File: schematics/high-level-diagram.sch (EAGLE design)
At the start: 2 parts

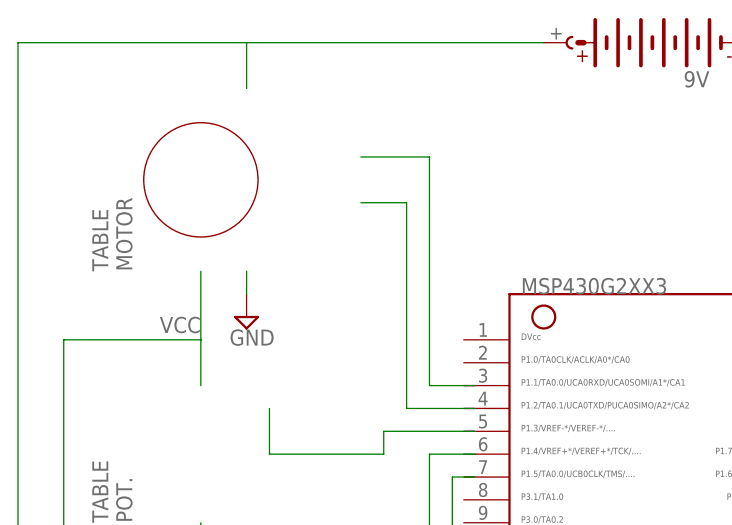
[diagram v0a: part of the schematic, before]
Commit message: Added button schematic and updated final report draft accordingly.  Adjusted high-level schematic accordingly.
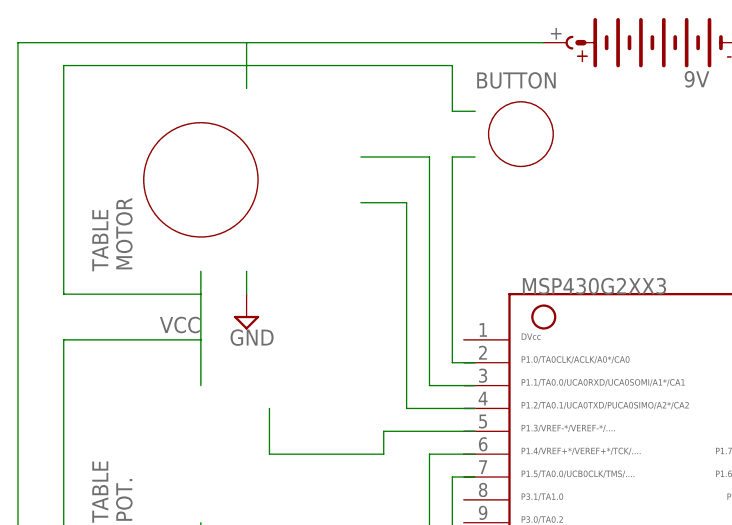
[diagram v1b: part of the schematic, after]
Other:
- note added: "BUTTON"
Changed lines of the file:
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@@
 <text x="-203.2" y="149.86" size="1.778" layer="95" rot="R90">WEAPON
 POT.</text>
+<frame x1="-165.1" y1="215.9" x2="-154.94" y2="226.06" columns="0" rows="0" layer="94" border-left="no" border-top="no" border-right="no" border-bottom="no"/>
+<circle x="-160.02" y="220.98" radius="3.5921" width="0.1524" layer="94"/>
+<text x="-165.1" y="226.06" size="1.778" layer="95">BUTTON</text>
 </plain>
 <instances>
@@
 <net name="VCC" class="0">
 <segment>
-<wire x1="-195.58" y1="205.74" x2="-195.58" y2="198.12" width="0.1524" layer="91"/>
+<wire x1="-195.58" y1="205.74" x2="-195.58" y2="203.2" width="0.1524" layer="91"/>
 <label x="-195.58" y="200.66" size="1.778" layer="95" rot="R180"/>
+<wire x1="-195.58" y1="203.2" x2="-195.58" y2="198.12" width="0.1524" layer="91"/>
 <wire x1="-195.58" y1="198.12" x2="-195.58" y2="193.04" width="0.1524" layer="91"/>
 <wire x1="-195.58" y1="198.12" x2="-210.82" y2="198.12" width="0.1524" layer="91"/>
@@
 <wire x1="-210.82" y1="167.64" x2="-195.58" y2="167.64" width="0.1524" layer="91"/>
 <wire x1="-195.58" y1="167.64" x2="-195.58" y2="165.1" width="0.1524" layer="91"/>
+<wire x1="-195.58" y1="203.2" x2="-210.82" y2="203.2" width="0.1524" layer="91"/>
+<wire x1="-210.82" y1="203.2" x2="-210.82" y2="228.6" width="0.1524" layer="91"/>
+<wire x1="-210.82" y1="228.6" x2="-167.64" y2="228.6" width="0.1524" layer="91"/>
+<wire x1="-167.64" y1="228.6" x2="-167.64" y2="223.52" width="0.1524" layer="91"/>
+<wire x1="-167.64" y1="223.52" x2="-165.1" y2="223.52" width="0.1524" layer="91"/>
 </segment>
 </net>
@@
 </segment>
 </net>
+<net name="N$4" class="0">
+<segment>
+<wire x1="-165.1" y1="218.44" x2="-167.64" y2="218.44" width="0.1524" layer="91"/>
+<wire x1="-167.64" y1="218.44" x2="-167.64" y2="195.58" width="0.1524" layer="91"/>
+<wire x1="-167.64" y1="195.58" x2="-165.1" y2="195.58" width="0.1524" layer="91"/>
+</segment>
+</net>

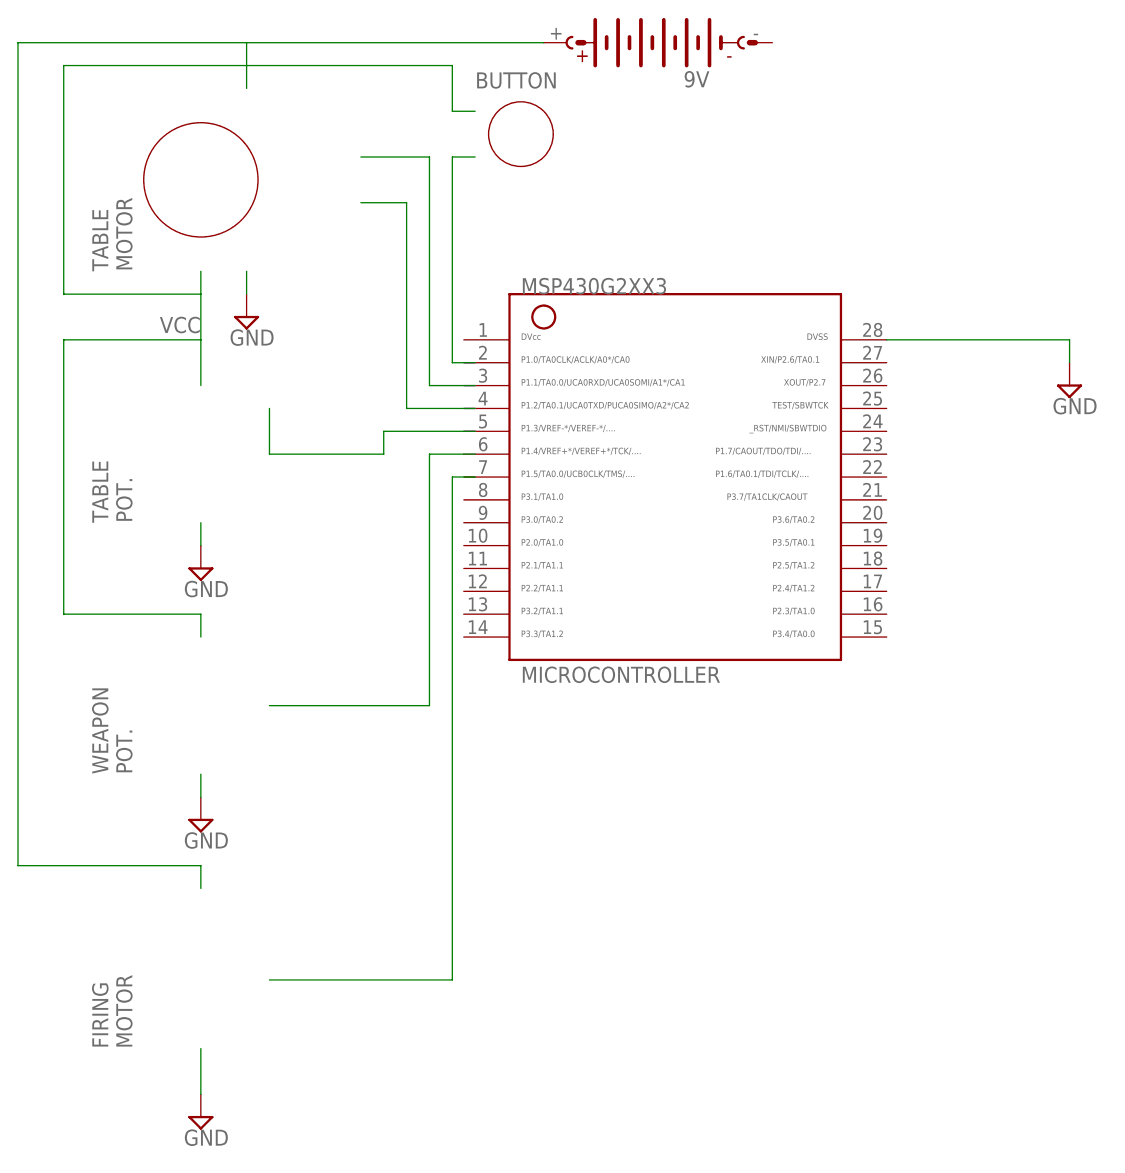
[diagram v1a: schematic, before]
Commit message: Updated schematics to have appropriate pins and to fit most recent updates.  Final report updated and ready for review.
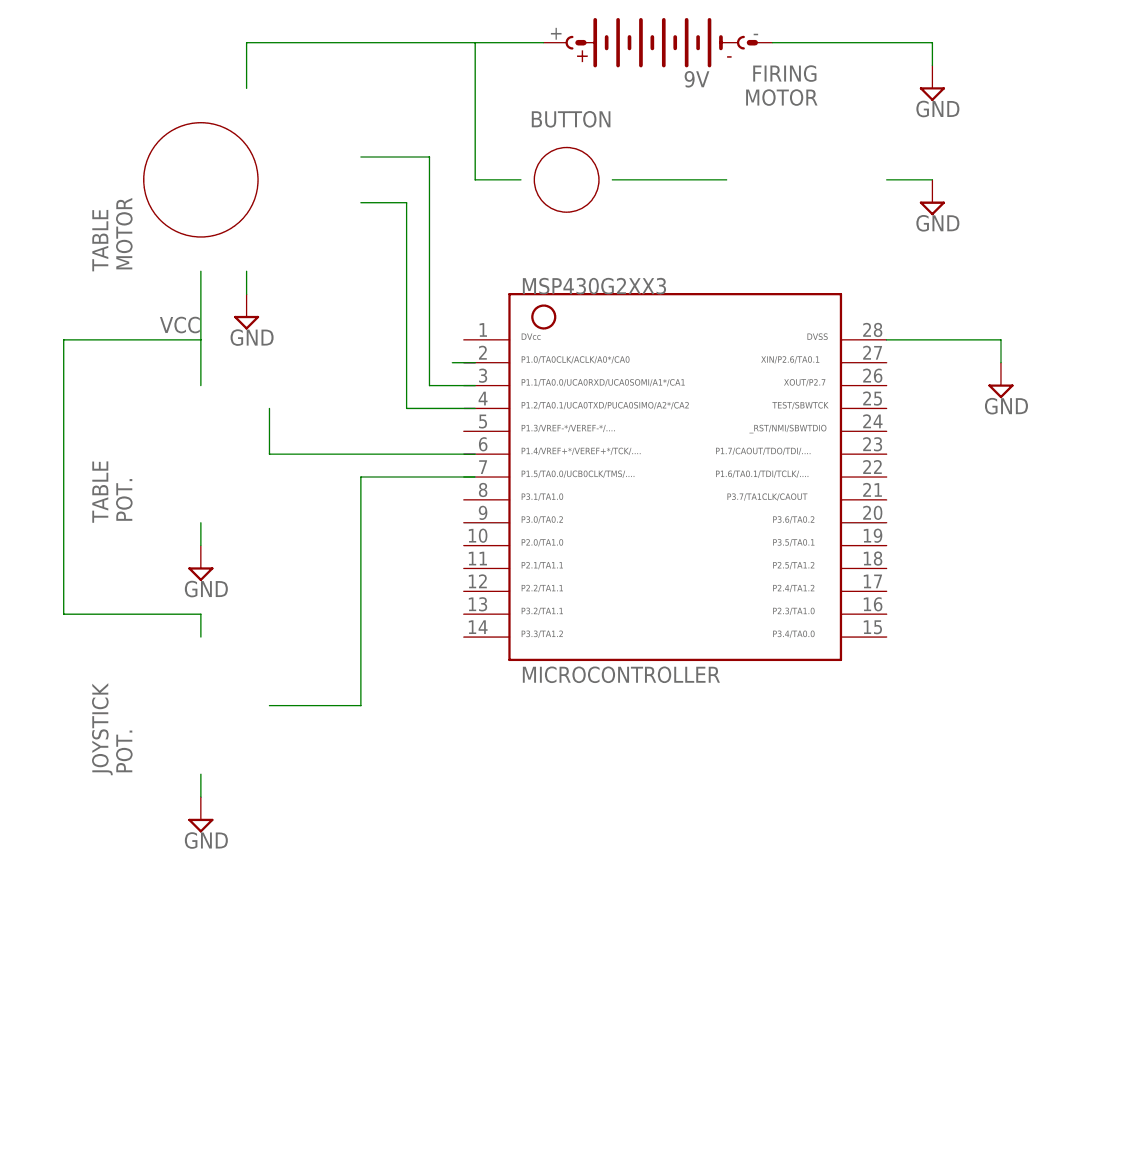
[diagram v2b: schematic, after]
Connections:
- net GND: now also 9V.-
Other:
- note added: "JOYSTICK POT."
- note removed: "WEAPON POT."
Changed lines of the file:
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@@
 <part name="SUPPLY1" library="supply2" deviceset="GND" device=""/>
 <part name="SUPPLY2" library="supply2" deviceset="GND" device=""/>
+<part name="SUPPLY3" library="supply2" deviceset="GND" device=""/>
 </parts>
 <sheets>
@@
 MOTOR</text>
 <circle x="-195.58" y="215.9" radius="6.35" width="0.1524" layer="94"/>
-<frame x1="-203.2" y1="119.38" x2="-187.96" y2="137.16" columns="0" rows="1" layer="94" border-left="no"/>
-<text x="-203.2" y="119.38" size="1.778" layer="95" rot="R90">FIRING
+<frame x1="-137.16" y1="208.28" x2="-119.38" y2="223.52" columns="0" rows="1" layer="94" border-right="no"/>
+<text x="-127" y="228.6" size="1.778" layer="95" rot="R180">FIRING
 MOTOR</text>
 <frame x1="-203.2" y1="177.8" x2="-187.96" y2="193.04" columns="0" rows="1" layer="94" border-left="no"/>
@@
 POT.</text>
 <frame x1="-203.2" y1="149.86" x2="-187.96" y2="165.1" columns="0" rows="1" layer="94" border-left="no"/>
-<text x="-203.2" y="149.86" size="1.778" layer="95" rot="R90">WEAPON
+<text x="-203.2" y="149.86" size="1.778" layer="95" rot="R90">JOYSTICK
 POT.</text>
-<frame x1="-165.1" y1="215.9" x2="-154.94" y2="226.06" columns="0" rows="0" layer="94" border-left="no" border-top="no" border-right="no" border-bottom="no"/>
-<circle x="-160.02" y="220.98" radius="3.5921" width="0.1524" layer="94"/>
-<text x="-165.1" y="226.06" size="1.778" layer="95">BUTTON</text>
+<frame x1="-160.02" y1="210.82" x2="-149.86" y2="220.98" columns="0" rows="0" layer="94" border-left="no" border-top="no" border-right="no" border-bottom="no"/>
+<circle x="-154.94" y="215.9" radius="3.5921" width="0.1524" layer="94"/>
+<text x="-149.86" y="223.52" size="1.778" layer="95" rot="R180">BUTTON</text>
 </plain>
 <instances>
 <instance part="MICROCONTROLLER" gate="G$1" x="-142.24" y="187.96"/>
-<instance part="SUPPLY7" gate="GND" x="-99.06" y="193.04"/>
+<instance part="SUPPLY7" gate="GND" x="-106.68" y="193.04"/>
 <instance part="9V" gate="G$1" x="-144.78" y="231.14" rot="R180"/>
 <instance part="SUPPLY15" gate="GND" x="-190.5" y="200.66"/>
-<instance part="SUPPLY16" gate="GND" x="-195.58" y="111.76"/>
+<instance part="SUPPLY16" gate="GND" x="-114.3" y="213.36"/>
 <instance part="SUPPLY1" gate="GND" x="-195.58" y="172.72"/>
 <instance part="SUPPLY2" gate="GND" x="-195.58" y="144.78"/>
+<instance part="SUPPLY3" gate="GND" x="-114.3" y="226.06"/>
 </instances>
 <busses>
@@
 <pinref part="MICROCONTROLLER" gate="G$1" pin="28"/>
 <pinref part="SUPPLY7" gate="GND" pin="GND"/>
-<wire x1="-119.38" y1="198.12" x2="-99.06" y2="198.12" width="0.1524" layer="91"/>
-<wire x1="-99.06" y1="198.12" x2="-99.06" y2="195.58" width="0.1524" layer="91"/>
+<wire x1="-119.38" y1="198.12" x2="-106.68" y2="198.12" width="0.1524" layer="91"/>
+<wire x1="-106.68" y1="198.12" x2="-106.68" y2="195.58" width="0.1524" layer="91"/>
 </segment>
 <segment>
@@
 <segment>
 <pinref part="SUPPLY16" gate="GND" pin="GND"/>
-<wire x1="-195.58" y1="119.38" x2="-195.58" y2="114.3" width="0.1524" layer="91"/>
+<wire x1="-119.38" y1="215.9" x2="-114.3" y2="215.9" width="0.1524" layer="91"/>
 </segment>
 <segment>
@@
 <wire x1="-195.58" y1="147.32" x2="-195.58" y2="149.86" width="0.1524" layer="91"/>
 </segment>
+<segment>
+<pinref part="9V" gate="G$1" pin="-"/>
+<wire x1="-132.08" y1="231.14" x2="-114.3" y2="231.14" width="0.1524" layer="91"/>
+<pinref part="SUPPLY3" gate="GND" pin="GND"/>
+<wire x1="-114.3" y1="231.14" x2="-114.3" y2="228.6" width="0.1524" layer="91"/>
+</segment>
 </net>
 <net name="VCC" class="0">
 <segment>
-<wire x1="-195.58" y1="205.74" x2="-195.58" y2="203.2" width="0.1524" layer="91"/>
 <label x="-195.58" y="200.66" size="1.778" layer="95" rot="R180"/>
-<wire x1="-195.58" y1="203.2" x2="-195.58" y2="198.12" width="0.1524" layer="91"/>
+<wire x1="-195.58" y1="205.74" x2="-195.58" y2="198.12" width="0.1524" layer="91"/>
 <wire x1="-195.58" y1="198.12" x2="-195.58" y2="193.04" width="0.1524" layer="91"/>
 <wire x1="-195.58" y1="198.12" x2="-210.82" y2="198.12" width="0.1524" layer="91"/>
@@
 <wire x1="-210.82" y1="167.64" x2="-195.58" y2="167.64" width="0.1524" layer="91"/>
 <wire x1="-195.58" y1="167.64" x2="-195.58" y2="165.1" width="0.1524" layer="91"/>
-<wire x1="-195.58" y1="203.2" x2="-210.82" y2="203.2" width="0.1524" layer="91"/>
-<wire x1="-210.82" y1="203.2" x2="-210.82" y2="228.6" width="0.1524" layer="91"/>
-<wire x1="-210.82" y1="228.6" x2="-167.64" y2="228.6" width="0.1524" layer="91"/>
-<wire x1="-167.64" y1="228.6" x2="-167.64" y2="223.52" width="0.1524" layer="91"/>
-<wire x1="-167.64" y1="223.52" x2="-165.1" y2="223.52" width="0.1524" layer="91"/>
 </segment>
 </net>
@@
 </segment>
 </net>
-<net name="N$27" class="0">
+<net name="N$5" class="0">
 <segment>
+<wire x1="-167.64" y1="195.58" x2="-165.1" y2="195.58" width="0.1524" layer="91"/>
+</segment>
+</net>
+<net name="N$6" class="0">
+<segment>
+<wire x1="-149.86" y1="215.9" x2="-137.16" y2="215.9" width="0.1524" layer="91"/>
+</segment>
+</net>
+<net name="N$4" class="0">
+<segment>
+<pinref part="9V" gate="G$1" pin="+"/>
+<wire x1="-190.5" y1="231.14" x2="-165.1" y2="231.14" width="0.1524" layer="91"/>
+<wire x1="-165.1" y1="231.14" x2="-157.48" y2="231.14" width="0.1524" layer="91"/>
 <wire x1="-190.5" y1="226.06" x2="-190.5" y2="231.14" width="0.1524" layer="91"/>
-<pinref part="9V" gate="G$1" pin="+"/>
-<wire x1="-190.5" y1="231.14" x2="-157.48" y2="231.14" width="0.1524" layer="91"/>
-<wire x1="-190.5" y1="231.14" x2="-215.9" y2="231.14" width="0.1524" layer="91"/>
-<wire x1="-215.9" y1="231.14" x2="-215.9" y2="139.7" width="0.1524" layer="91"/>
-<wire x1="-215.9" y1="139.7" x2="-195.58" y2="139.7" width="0.1524" layer="91"/>
-<wire x1="-195.58" y1="139.7" x2="-195.58" y2="137.16" width="0.1524" layer="91"/>
+<wire x1="-165.1" y1="231.14" x2="-165.1" y2="215.9" width="0.1524" layer="91"/>
+<wire x1="-165.1" y1="215.9" x2="-160.02" y2="215.9" width="0.1524" layer="91"/>
+</segment>
+</net>
+<net name="N$8" class="0">
+<segment>
+<wire x1="-187.96" y1="185.42" x2="-187.96" y2="190.5" width="0.1524" layer="91"/>
+<wire x1="-165.1" y1="185.42" x2="-187.96" y2="185.42" width="0.1524" layer="91"/>
 </segment>
 </net>
 <net name="N$1" class="0">
 <segment>
-<wire x1="-187.96" y1="185.42" x2="-187.96" y2="190.5" width="0.1524" layer="91"/>
-<wire x1="-187.96" y1="185.42" x2="-175.26" y2="185.42" width="0.1524" layer="91"/>
-<wire x1="-175.26" y1="185.42" x2="-175.26" y2="187.96" width="0.1524" layer="91"/>
-<wire x1="-165.1" y1="187.96" x2="-175.26" y2="187.96" width="0.1524" layer="91"/>
+<wire x1="-187.96" y1="157.48" x2="-177.8" y2="157.48" width="0.1524" layer="91"/>
+<wire x1="-177.8" y1="157.48" x2="-177.8" y2="182.88" width="0.1524" layer="91"/>
+<wire x1="-177.8" y1="182.88" x2="-165.1" y2="182.88" width="0.1524" layer="91"/>
 </segment>
 </net>
-<net name="N$2" class="0">
-<segment>
-<wire x1="-187.96" y1="157.48" x2="-170.18" y2="157.48" width="0.1524" layer="91"/>
-<wire x1="-170.18" y1="157.48" x2="-170.18" y2="185.42" width="0.1524" layer="91"/>
-<wire x1="-170.18" y1="185.42" x2="-165.1" y2="185.42" width="0.1524" layer="91"/>
-</segment>
-</net>
-<net name="N$3" class="0">
-<segment>
-<wire x1="-187.96" y1="127" x2="-167.64" y2="127" width="0.1524" layer="91"/>
-<wire x1="-167.64" y1="127" x2="-167.64" y2="182.88" width="0.1524" layer="91"/>
-<wire x1="-167.64" y1="182.88" x2="-165.1" y2="182.88" width="0.1524" layer="91"/>
-</segment>
-</net>
-<net name="N$4" class="0">
-<segment>
-<wire x1="-165.1" y1="218.44" x2="-167.64" y2="218.44" width="0.1524" layer="91"/>
-<wire x1="-167.64" y1="218.44" x2="-167.64" y2="195.58" width="0.1524" layer="91"/>
-<wire x1="-167.64" y1="195.58" x2="-165.1" y2="195.58" width="0.1524" layer="91"/>
-</segment>
-</net>
